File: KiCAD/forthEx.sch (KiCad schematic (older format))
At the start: 61 parts, among them CON1 SD_Card, CON2 BARREL_JACK 2,1mm, J1 RCA_JACK, J2 RCA_JACK, J3 RJ12, P1 ICSP, Q1 2N3906, Q2 2N3904, SW1 Power, SW2 reset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

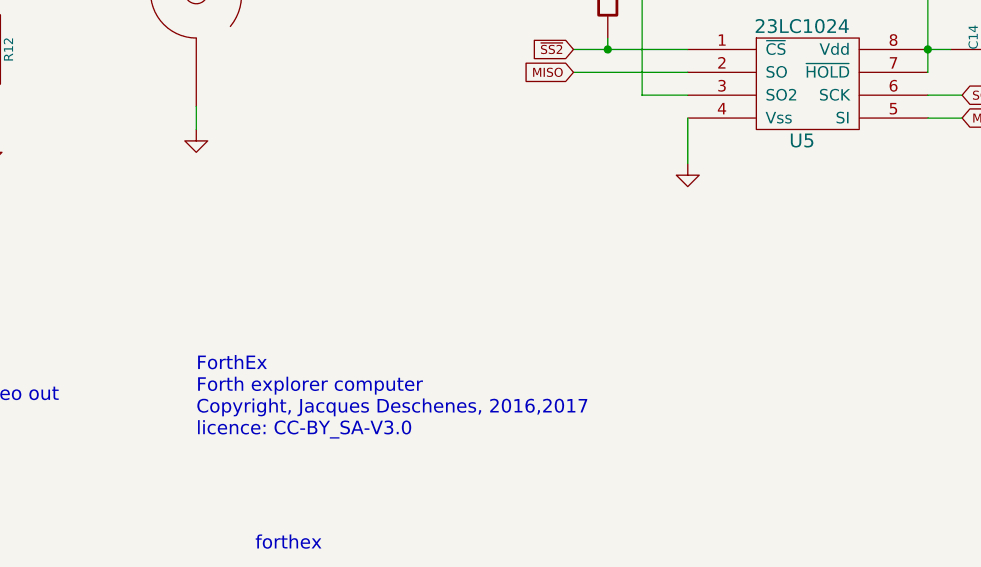
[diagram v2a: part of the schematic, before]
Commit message: Modifiez encore le générateur vidéo pour vérifier s'il est nécessaire d'inclure un seuil de noir comme indiqué dans la spécification NTSC. Si ça peut fonctionner sans seuil de noir je pourrai libéré la broche 12 du MCU. CONCLUSION: Sans fonctionne très bien sans seuil de noir.
Correction bogue dans serial.s (non résolu à ce moment).
Travail dans vt102.s
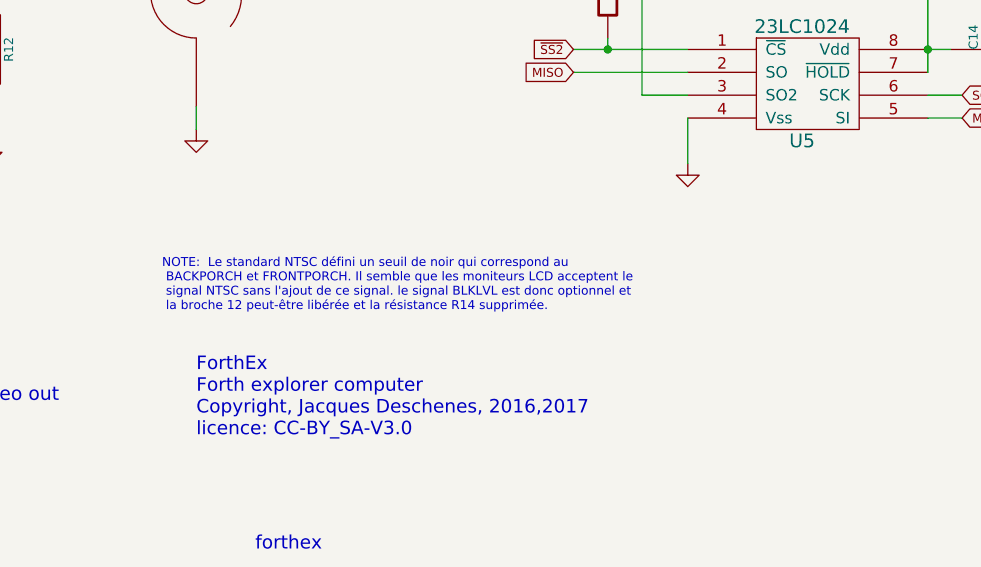
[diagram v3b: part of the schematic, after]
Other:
- note added: "NOTE: Le standard NTSC défini un seuil de noir qui correspond au\n BACKPORCH et FRONTPORCH. Il semble que les moniteurs LCD acceptent le\n signal NTSC sans l'ajout de ce signal. le signal BLKLVL est donc optionnel et\n la broche 12 peut-être libérée et la résistance R14 supprimée."
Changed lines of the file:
@@
 Wire Wire Line
 	4950 3450 5200 3450
+Text Notes 7050 6450 0    39   ~ 0
+NOTE:  Le standard NTSC défini un seuil de noir qui correspond au\n BACKPORCH et FRONTPORCH. Il semble que les moniteurs LCD acceptent le\n signal NTSC sans l'ajout de ce signal. le signal BLKLVL est donc optionnel et\n la broche 12 peut-être libérée et la résistance R14 supprimée.
 $EndSCHEMATC

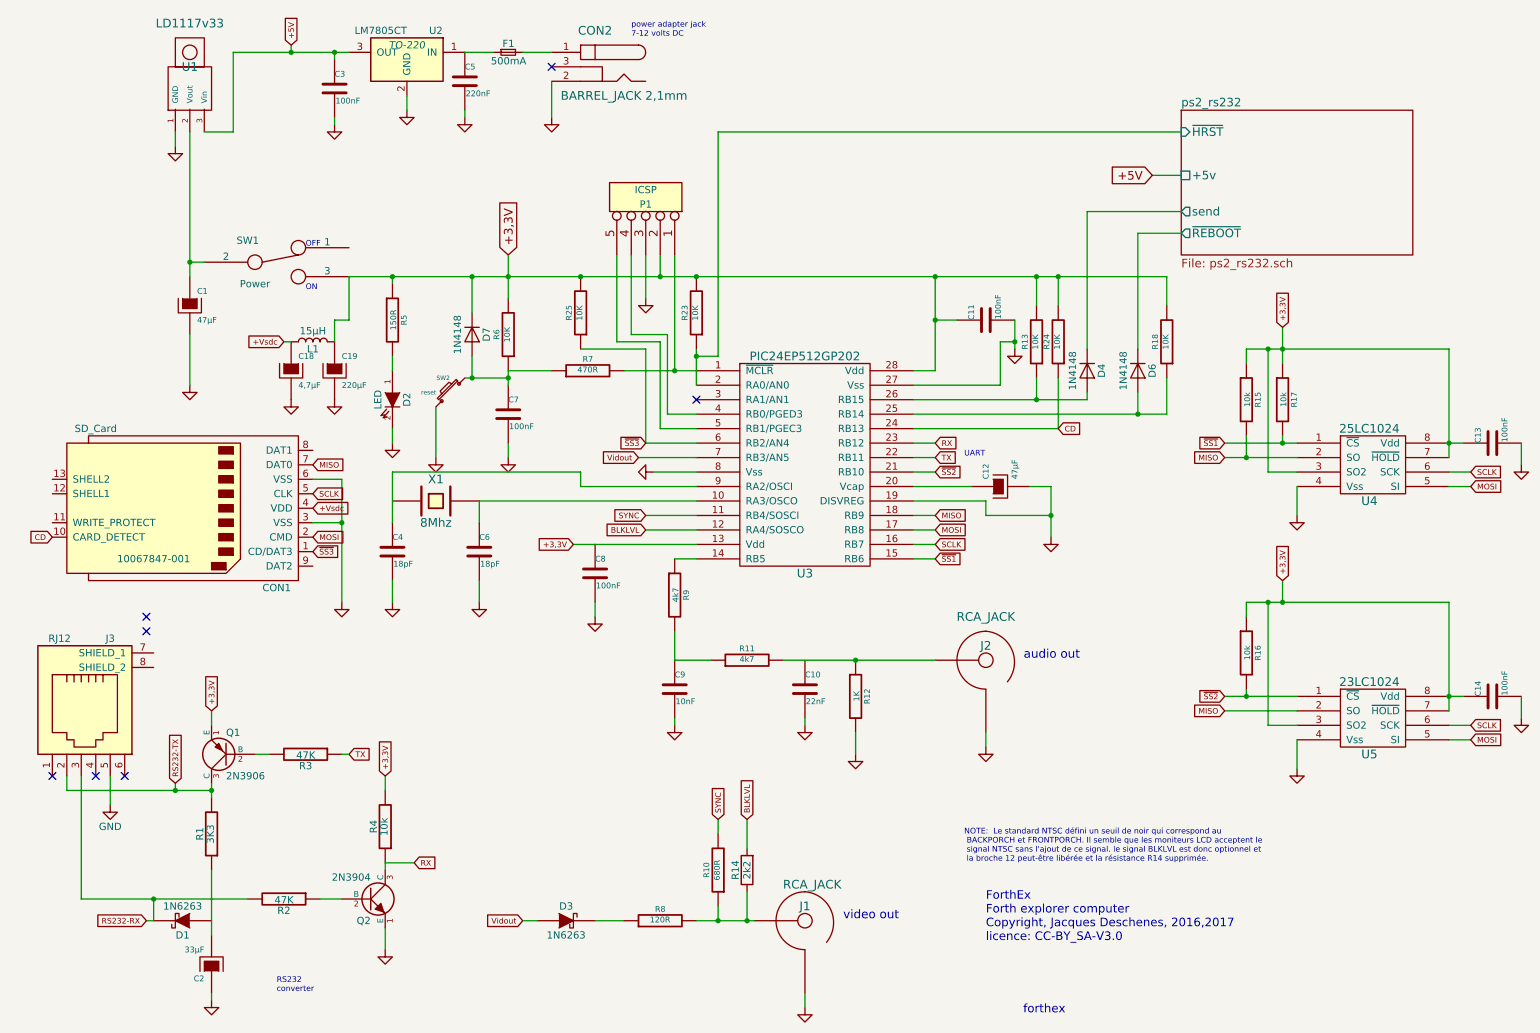
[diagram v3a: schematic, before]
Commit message: Modification matériel circuit port rs-232. Tentative de débogage port rs-232.
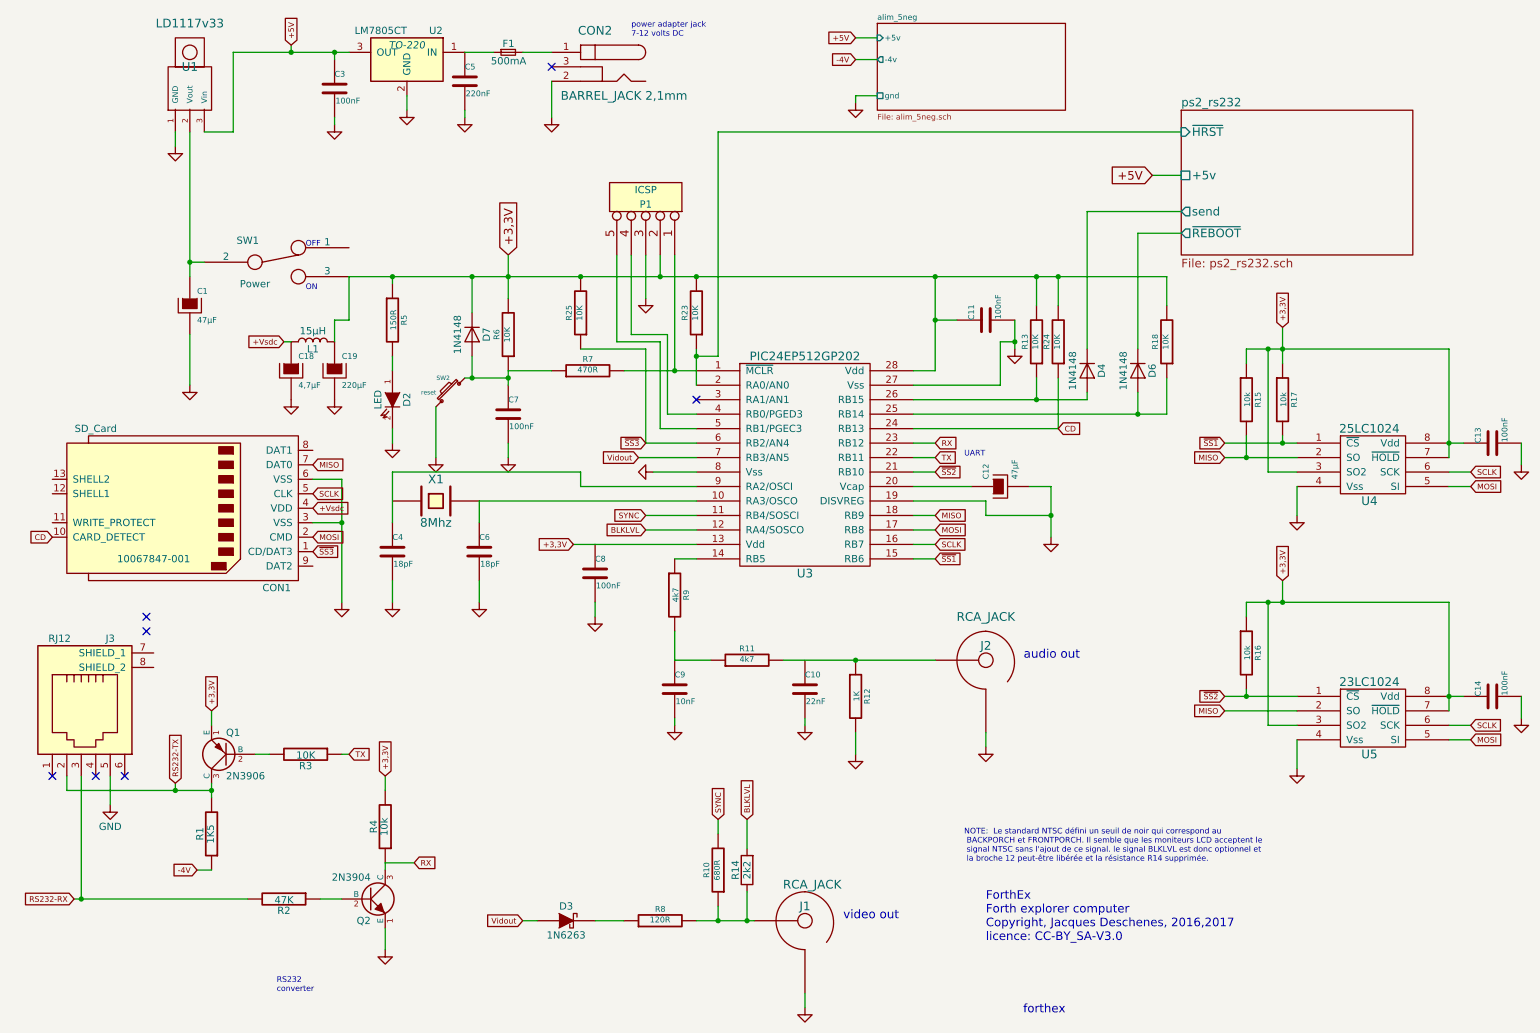
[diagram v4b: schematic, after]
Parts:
- removed C2: 33µF, ~, symbol CAPAPOL
- removed D1: 1N6263, symbol DIODESCH
- R1: value 3K3 -> 1K5
- R3: value 47K -> 10K
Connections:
- net -4V: now reaches R1.1
